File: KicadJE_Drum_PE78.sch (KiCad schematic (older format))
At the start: 112 parts, among them U101 74HC04

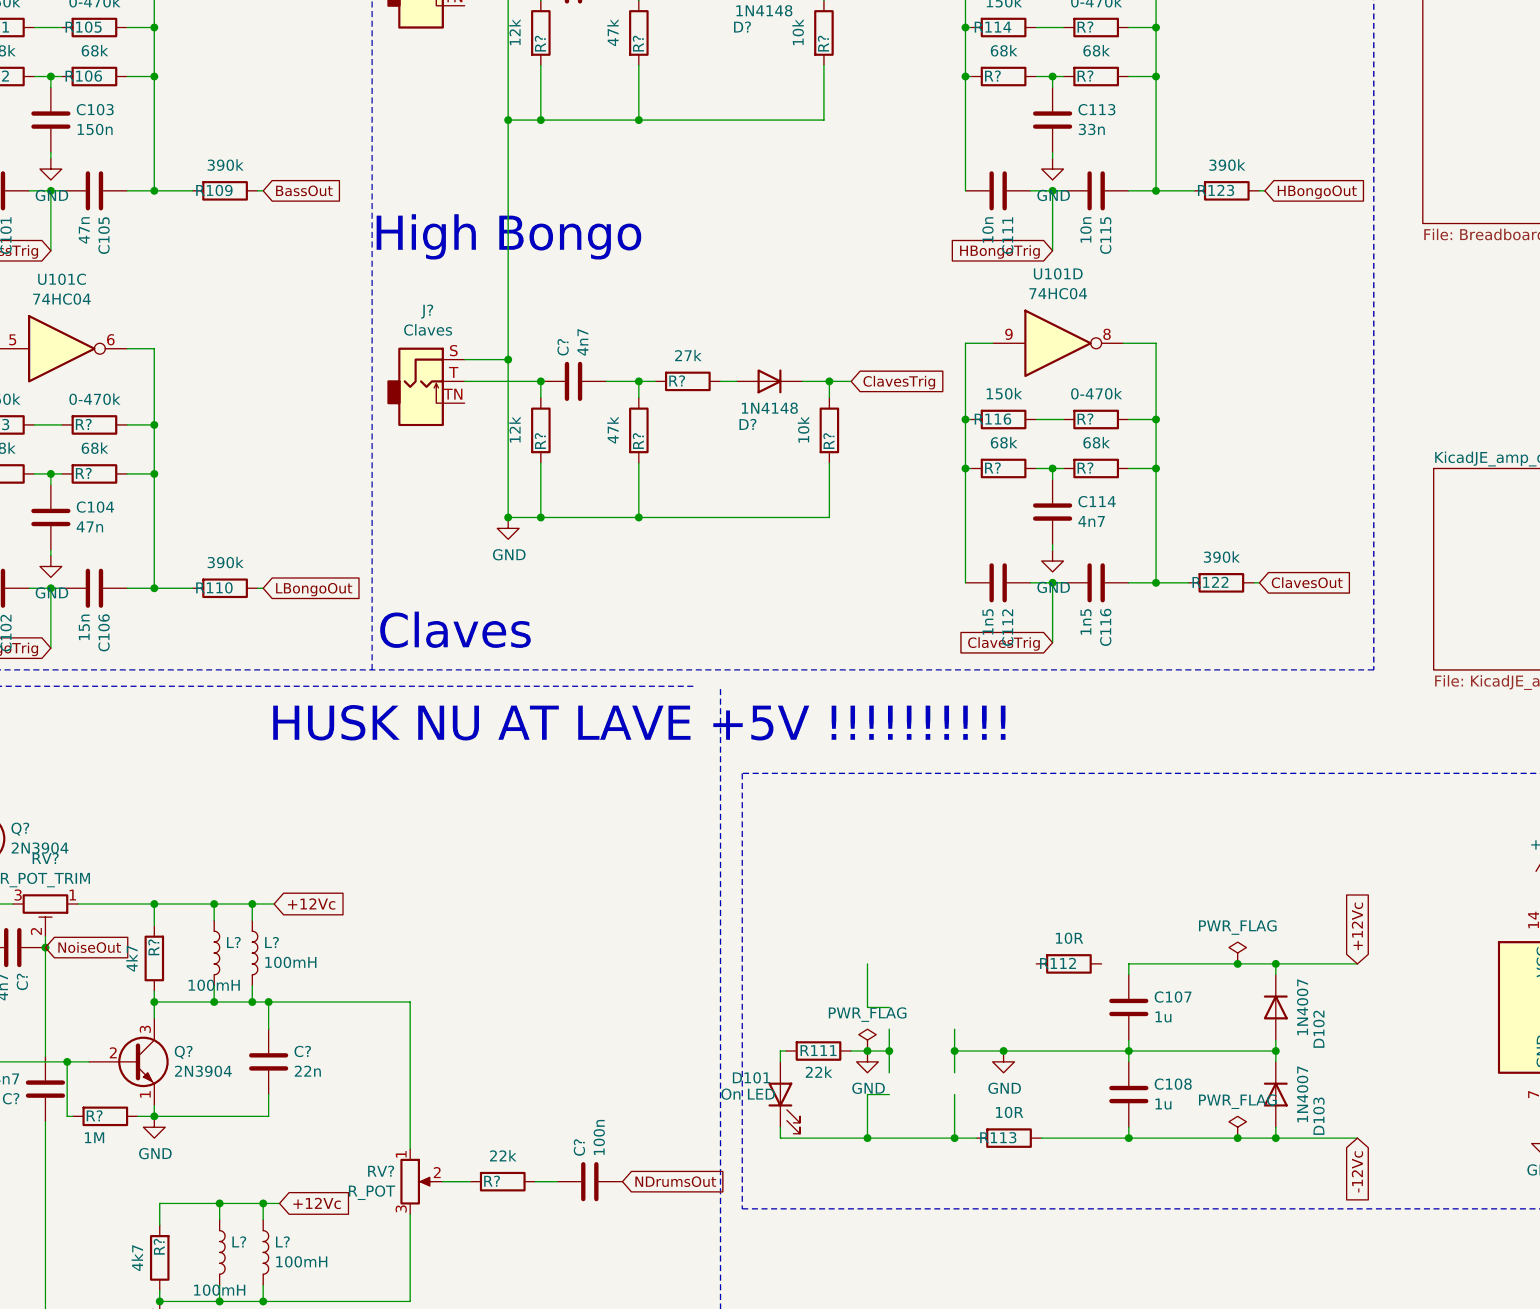
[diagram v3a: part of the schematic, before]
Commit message: Amp out
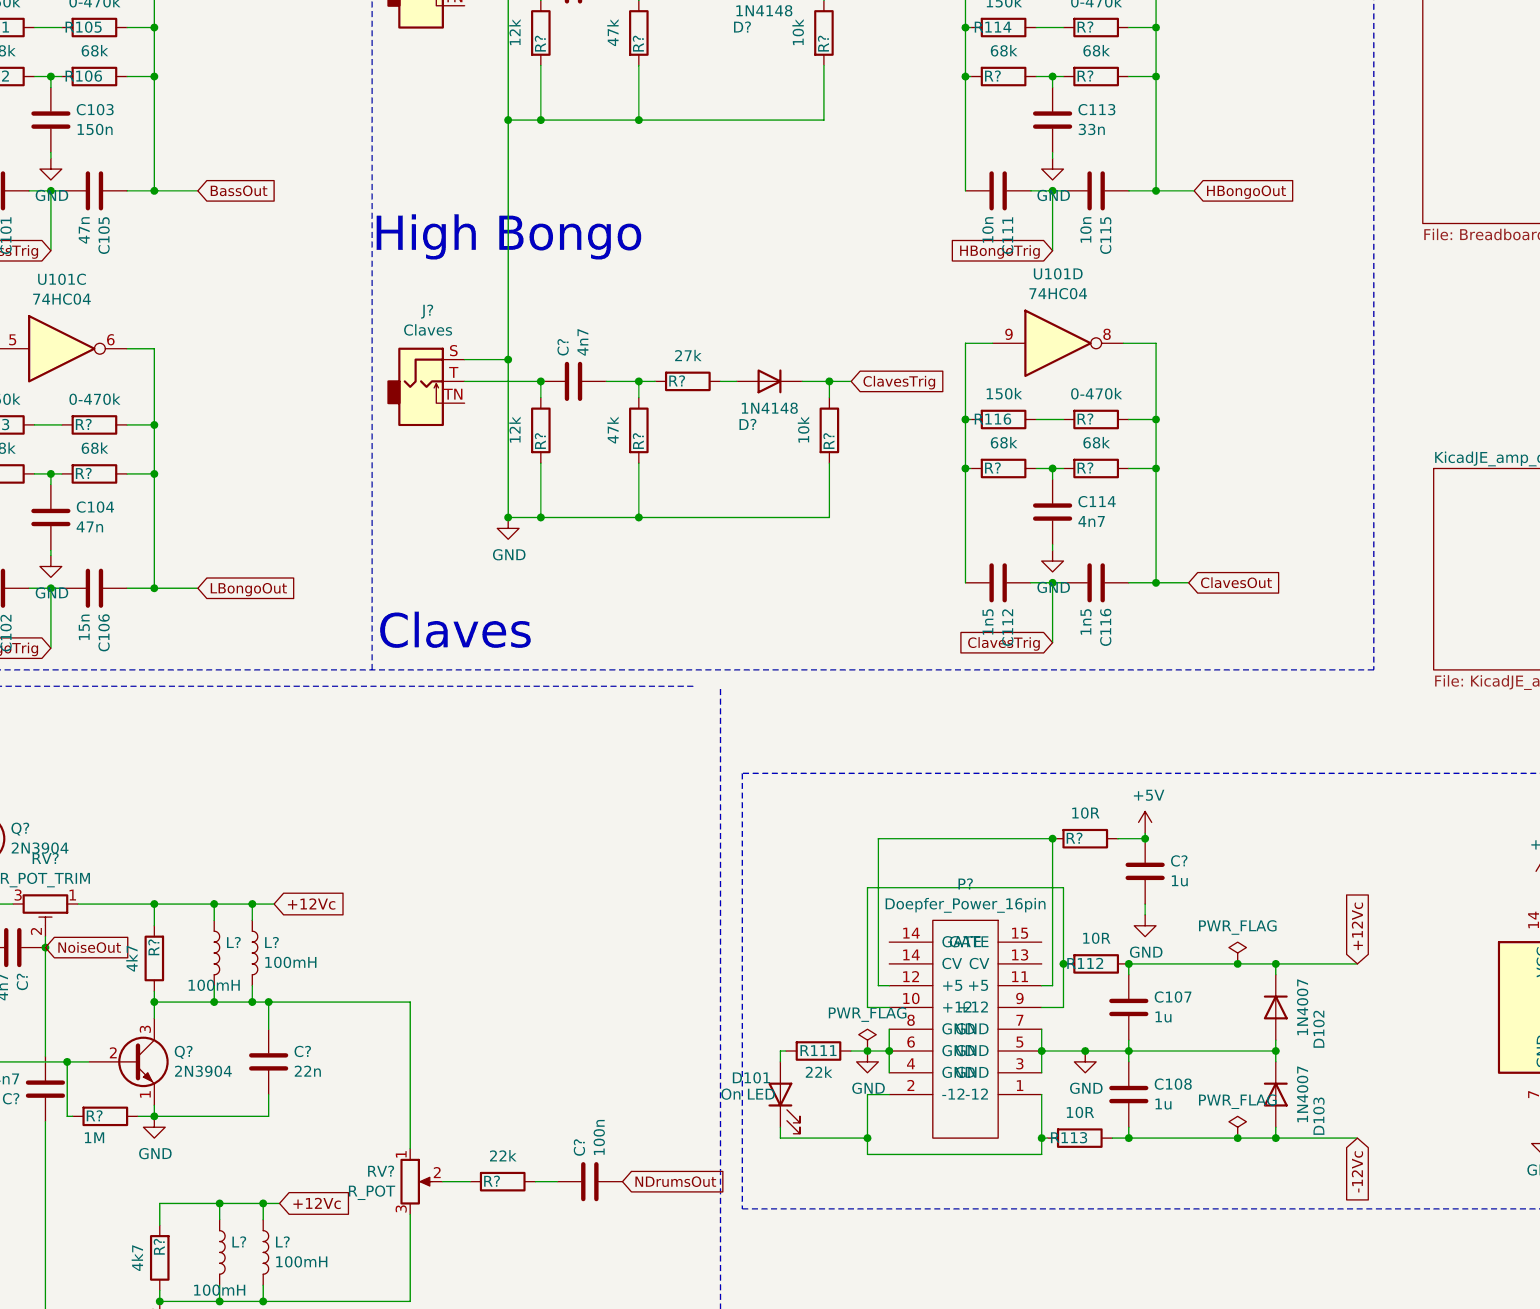
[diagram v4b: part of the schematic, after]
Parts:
- removed R109, R110, R122, R123: 390k, AJ:R_0805_AJ, symbol Device:R
- added C?: 1u, Capacitor_SMD:C_1206_3216Metric_Pad1.42x1.75mm_HandSolder, symbol Device:C
- added P?: Doepfer_Power_16pin, Connector_PinHeader_2.54mm:PinHeader_2x08_P2.54mm_Vertical, symbol Doepfer_Power_14pin:Doepfer_Power_16pin
- added R?: 10R, AJ:R_0805_AJ, symbol Device:R
- RV?: footprint (none) -> AJ:Potentiometer_China_RK09_Single_Vertical_AJ
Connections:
- net +12Vc: now also R112.1
- net +5V: now also C?.1, R?.1
- net BassOut: now also C105.1, R105.1, R106.1, U101.2
- net ClavesOut: now also C116.1, R?.1, R?.1, U101.8
- net GND: now also C?.2, P?.3 (GND), P?.4 (GND), P?.5 (GND), P?.6 (GND), P?.7 (GND), P?.8 (GND)
- net HBongoOut: now also C115.1, R?.1, R?.1, U101.4
- net LBongoOut: now also C106.1, R?.1, R?.1, U101.6
- net at D101.1 (K), R113.2: now also P?.1 (-12), P?.2 (-12)
- net at R112.2: now also P?.10 (+12), P?.9 (+12)
- new net: P?.11 (+5), P?.12 (+5), R?.2
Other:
- moved on the sheet: R112, R113
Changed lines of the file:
@@
 L Device:R R113
 U 1 1 605ABB0A
-P 8225 6175
+P 8550 6175
 AR Path="/605ABB0A" Ref="R113"  Part="1"
 AR Path="/5C8C5FC0/605ABB0A" Ref="R?"  Part="1"
 AR Path="/5D60ED9A/605ABB0A" Ref="R?"  Part="1"
 AR Path="/60565919/605ABB0A" Ref="R?"  Part="1"
-F 0 "R113" V 8225 6125 50  0000 C CNN
-F 1 "10R" V 8109 6175 50  0000 C CNN
-F 2 "AJ:R_0805_AJ" V 8155 6175 50  0001 C CNN
-F 3 "~" H 8225 6175 50  0001 C CNN
-	1    8225 6175
+F 0 "R113" V 8550 6125 50  0000 C CNN
+F 1 "10R" V 8434 6175 50  0000 C CNN
+F 2 "AJ:R_0805_AJ" V 8480 6175 50  0001 C CNN
+F 3 "~" H 8550 6175 50  0001 C CNN
+	1    8550 6175
 	0    1    1    0
 $EndComp
@@
 L Device:R R112
 U 1 1 605ABB10
-P 8500 5375
+P 8625 5375
 AR Path="/605ABB10" Ref="R112"  Part="1"
 AR Path="/5C8C5FC0/605ABB10" Ref="R?"  Part="1"
 AR Path="/5D60ED9A/605ABB10" Ref="R?"  Part="1"
 AR Path="/60565919/605ABB10" Ref="R?"  Part="1"
-F 0 "R112" V 8500 5325 50  0000 C CNN
-F 1 "10R" V 8384 5375 50  0000 C CNN
-F 2 "AJ:R_0805_AJ" V 8430 5375 50  0001 C CNN
-F 3 "~" H 8500 5375 50  0001 C CNN
-	1    8500 5375
+F 0 "R112" V 8625 5325 50  0000 C CNN
+F 1 "10R" V 8509 5375 50  0000 C CNN
+F 2 "AJ:R_0805_AJ" V 8555 5375 50  0001 C CNN
+F 3 "~" H 8625 5375 50  0001 C CNN
+	1    8625 5375
 	0    1    1    0
 $EndComp
@@
 Wire Wire Line
 	7575 5775 7675 5775
-Wire Wire Line
-	7975 5775 8200 5775
 Text GLabel 9825 6175 3    50   Input ~ 0
 -12Vc
@@
 Wire Wire Line
 	8775 5425 8775 5375
-Wire Wire Line
-	8375 6175 8775 6175
-Connection ~ 8775 6175
 Wire Wire Line
 	8775 6125 8775 6175
@@
 $EndComp
 Wire Wire Line
-	7975 6175 8075 6175
-Connection ~ 7975 6175
-Wire Wire Line
-	7975 5975 7975 6175
-Wire Wire Line
-	7975 5775 7975 5675
-Connection ~ 7975 5775
-Wire Wire Line
-	7975 5875 7975 5775
+	8375 5775 8375 5675
+Connection ~ 8375 5775
+Wire Wire Line
+	8375 5875 8375 5775
 Wire Wire Line
 	7675 5775 7675 5675
@@
 	7175 6175 7575 6175
 Wire Wire Line
-	7575 6175 7975 6175
-Connection ~ 7575 6175
-Wire Wire Line
 	7575 5975 7575 6175
 Wire Wire Line
 	7675 5975 7575 5975
-Wire Wire Line
-	7575 5575 7575 5375
 Wire Wire Line
 	7675 5575 7575 5575
@@
 L power:GND #PWR0104
 U 1 1 6076279B
-P 8200 5775
-F 0 "#PWR0104" H 8200 5525 50  0001 C CNN
-F 1 "GND" H 8205 5602 50  0000 C CNN
-F 2 "" H 8200 5775 50  0001 C CNN
-F 3 "" H 8200 5775 50  0001 C CNN
-	1    8200 5775
+P 8575 5775
+F 0 "#PWR0104" H 8575 5525 50  0001 C CNN
+F 1 "GND" H 8580 5602 50  0000 C CNN
+F 2 "" H 8575 5775 50  0001 C CNN
+F 3 "" H 8575 5775 50  0001 C CNN
+	1    8575 5775
 	1    0    0    -1
 $EndComp
@@
 	1    0    0    -1
 $EndComp
-Connection ~ 8200 5775
-Wire Wire Line
-	8200 5775 8775 5775
 $Comp
 L 74xx:74HC04 U101
@@
 Wire Wire Line
 	8425 3625 8325 3625
-Text GLabel 4800 1825 2    47   Input ~ 0
+Text GLabel 4500 1825 2    47   Input ~ 0
 BassOut
-Wire Wire Line
-	4300 1825 4475 1825
 Connection ~ 4300 1825
-$Comp
-L Device:R R109
-U 1 1 607BE08D
-P 4625 1825
-AR Path="/607BE08D" Ref="R109"  Part="1"
-AR Path="/5C8C5FC0/607BE08D" Ref="R?"  Part="1"
-AR Path="/5D60ED9A/607BE08D" Ref="R?"  Part="1"
-AR Path="/60565919/607BE08D" Ref="R?"  Part="1"
-F 0 "R109" V 4625 1775 50  0000 C CNN
-F 1 "390k" V 4509 1825 50  0000 C CNN
-F 2 "AJ:R_0805_AJ" V 4555 1825 50  0001 C CNN
-F 3 "~" H 4625 1825 50  0001 C CNN
-	1    4625 1825
-	0    1    1    0
-$EndComp
-Wire Wire Line
-	4775 1825 4800 1825
 $Comp
 L Device:R R103
@@
 Wire Wire Line
 	3825 3650 3725 3650
-Text GLabel 4800 3650 2    47   Input ~ 0
+Text GLabel 4500 3650 2    47   Input ~ 0
 LBongoOut
-Wire Wire Line
-	4300 3650 4475 3650
 Connection ~ 4300 3650
-$Comp
-L Device:R R110
-U 1 1 607C1D57
-P 4625 3650
-AR Path="/607C1D57" Ref="R110"  Part="1"
-AR Path="/5C8C5FC0/607C1D57" Ref="R?"  Part="1"
-AR Path="/5D60ED9A/607C1D57" Ref="R?"  Part="1"
-AR Path="/60565919/607C1D57" Ref="R?"  Part="1"
-F 0 "R110" V 4625 3600 50  0000 C CNN
-F 1 "390k" V 4509 3650 50  0000 C CNN
-F 2 "AJ:R_0805_AJ" V 4555 3650 50  0001 C CNN
-F 3 "~" H 4625 3650 50  0001 C CNN
-	1    4625 3650
-	0    1    1    0
-$EndComp
-Wire Wire Line
-	4775 3650 4800 3650
 Wire Wire Line
 	3425 2550 3575 2550
 Wire Wire Line
 	4175 2550 4300 2550
-Text GLabel 9400 1825 2    47   Input ~ 0
+Text GLabel 9075 1825 2    47   Input ~ 0
 HBongoOut
 Wire Wire Line
 	8900 1825 9075 1825
-$Comp
-L Device:R R123
-U 1 1 607D73A4
-P 9225 1825
-AR Path="/607D73A4" Ref="R123"  Part="1"
-AR Path="/5C8C5FC0/607D73A4" Ref="R?"  Part="1"
-AR Path="/5D60ED9A/607D73A4" Ref="R?"  Part="1"
-AR Path="/60565919/607D73A4" Ref="R?"  Part="1"
-F 0 "R123" V 9225 1775 50  0000 C CNN
-F 1 "390k" V 9109 1825 50  0000 C CNN
-F 2 "AJ:R_0805_AJ" V 9155 1825 50  0001 C CNN
-F 3 "~" H 9225 1825 50  0001 C CNN
-	1    9225 1825
-	0    1    1    0
-$EndComp
-Wire Wire Line
-	9375 1825 9400 1825
 Connection ~ 8900 1825
 Wire Wire Line
@@
 Wire Wire Line
 	8750 2525 8900 2525
-Text GLabel 9375 3625 2    47   Input ~ 0
+Text GLabel 9050 3625 2    47   Input ~ 0
 ClavesOut
-$Comp
-L Device:R R122
-U 1 1 607F00E5
-P 9200 3625
-AR Path="/607F00E5" Ref="R122"  Part="1"
-AR Path="/5C8C5FC0/607F00E5" Ref="R?"  Part="1"
-AR Path="/5D60ED9A/607F00E5" Ref="R?"  Part="1"
-AR Path="/60565919/607F00E5" Ref="R?"  Part="1"
-F 0 "R122" V 9200 3575 50  0000 C CNN
-F 1 "390k" V 9084 3625 50  0000 C CNN
-F 2 "AJ:R_0805_AJ" V 9130 3625 50  0001 C CNN
-F 3 "~" H 9200 3625 50  0001 C CNN
-	1    9200 3625
-	0    1    1    0
-$EndComp
-Wire Wire Line
-	9350 3625 9375 3625
 Wire Wire Line
 	9050 3625 8900 3625
@@
 $EndComp
 Wire Wire Line
-	8775 5775 9450 5775
-Wire Wire Line
 	8775 5375 9275 5375
 Wire Wire Line
@@
 L power:+5V #PWR?
 U 1 1 60DE30BF
-P 10675 5000
-F 0 "#PWR?" H 10675 4850 50  0001 C CNN
-F 1 "+5V" H 10690 5173 50  0000 C CNN
-F 2 "" H 10675 5000 50  0001 C CNN
-F 3 "" H 10675 5000 50  0001 C CNN
-	1    10675 5000
+P 8850 4775
+F 0 "#PWR?" H 8850 4625 50  0001 C CNN
+F 1 "+5V" H 8865 4948 50  0000 C CNN
+F 2 "" H 8850 4775 50  0001 C CNN
+F 3 "" H 8850 4775 50  0001 C CNN
+	1    8850 4775
 	1    0    0    -1
 $EndComp
@@
 	10675 6150 10675 6075
 Text Notes 5000 8950 0    157  ~ 0
-HUSK NU AT LAVE +5V !!!!!!!!!!
-Text Notes 4825 4375 0    157  ~ 0
 HUSK NU AT LAVE +5V !!!!!!!!!!
 $Comp
@@
 F 0 "RV?" H 5406 6421 50  0000 R CNN
 F 1 "R_POT" H 5406 6330 50  0000 R CNN
-F 2 "" H 5475 6375 50  0001 C CNN
+F 2 "AJ:Potentiometer_China_RK09_Single_Vertical_AJ" H 5475 6375 50  0001 C CNN
 F 3 "~" H 5475 6375 50  0001 C CNN
 	1    5475 6375
@@
 Wire Wire Line
 	4800 6475 4875 6475
+$Comp
+L Doepfer_Power_14pin:Doepfer_Power_16pin P?
+U 1 1 61739A83
+P 8025 5675
+F 0 "P?" H 8025 5010 50  0000 C CNN
+F 1 "Doepfer_Power_16pin" H 8025 5101 50  0000 C CNN
+F 2 "Connector_PinHeader_2.54mm:PinHeader_2x08_P2.54mm_Vertical" H 8025 5675 50  0001 C CNN
+F 3 "DOCUMENTATION" H 8025 5675 50  0001 C CNN
+	1    8025 5675
+	-1   0    0    1
+$EndComp
+Connection ~ 8775 5375
+Wire Wire Line
+	8575 5775 8775 5775
+Wire Wire Line
+	8775 5775 9450 5775
+Wire Wire Line
+	8375 5775 8575 5775
+Connection ~ 8575 5775
+Wire Wire Line
+	8775 6175 8700 6175
+Connection ~ 8775 6175
+Wire Wire Line
+	8400 6175 8375 6175
+Wire Wire Line
+	8375 6175 8375 5975
+Wire Wire Line
+	7575 6175 7575 6250
+Wire Wire Line
+	7575 6250 8375 6250
+Wire Wire Line
+	8375 6250 8375 6175
+Connection ~ 7575 6175
+Connection ~ 8375 6175
+Wire Wire Line
+	8375 5575 8475 5575
+Wire Wire Line
+	8475 5575 8475 5375
+Wire Wire Line
+	7575 5025 8475 5025
+Wire Wire Line
+	8475 5025 8475 5375
+Wire Wire Line
+	7575 5025 7575 5575
+Connection ~ 8475 5375
+$Comp
+L Device:R R?
+U 1 1 619774B5
+P 8575 4800
+AR Path="/619774B5" Ref="R?"  Part="1"
+AR Path="/5C8C5FC0/619774B5" Ref="R?"  Part="1"
+AR Path="/5D60ED9A/619774B5" Ref="R?"  Part="1"
+AR Path="/60565919/619774B5" Ref="R?"  Part="1"
+F 0 "R?" V 8575 4750 50  0000 C CNN
+F 1 "10R" V 8459 4800 50  0000 C CNN
+F 2 "AJ:R_0805_AJ" V 8505 4800 50  0001 C CNN
+F 3 "~" H 8575 4800 50  0001 C CNN
+	1    8575 4800
+	0    1    1    0
+$EndComp
+Wire Wire Line
+	7675 5475 7625 5475
+Wire Wire Line
+	7625 5475 7625 4800
+Wire Wire Line
+	8375 5475 8425 5475
+Wire Wire Line
+	8425 4800 8425 5475
+Connection ~ 8425 4800
+Wire Wire Line
+	7625 4800 8425 4800
+Wire Wire Line
+	8725 4800 8850 4800
+Wire Wire Line
+	8850 4800 8850 4775
+$Comp
+L Device:C C?
+U 1 1 61A3ECD2
+P 8850 4950
+F 0 "C?" H 8965 4996 50  0000 L CNN
+F 1 "1u" H 8965 4905 50  0000 L CNN
+F 2 "Capacitor_SMD:C_1206_3216Metric_Pad1.42x1.75mm_HandSolder" H 8888 4800 50  0001 C CNN
+F 3 "~" H 8850 4950 50  0001 C CNN
+	1    8850 4950
+	1    0    0    -1
+$EndComp
+Connection ~ 8850 4800
+$Comp
+L power:GND #PWR?
+U 1 1 61A3F1FE
+P 8850 5150
+F 0 "#PWR?" H 8850 4900 50  0001 C CNN
+F 1 "GND" H 8855 4977 50  0000 C CNN
+F 2 "" H 8850 5150 50  0001 C CNN
+F 3 "" H 8850 5150 50  0001 C CNN
+	1    8850 5150
+	1    0    0    -1
+$EndComp
+Wire Wire Line
+	8850 5150 8850 5100
+$Comp
+L power:+5V #PWR?
+U 1 1 61A81B6C
+P 10675 5000
+F 0 "#PWR?" H 10675 4850 50  0001 C CNN
+F 1 "+5V" H 10690 5173 50  0000 C CNN
+F 2 "" H 10675 5000 50  0001 C CNN
+F 3 "" H 10675 5000 50  0001 C CNN
+	1    10675 5000
+	1    0    0    -1
+$EndComp
+Wire Wire Line
+	4300 1825 4500 1825
+Wire Wire Line
+	4300 3650 4500 3650
 $EndSCHEMATC

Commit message: Update misc diags
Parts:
- added C?: 100n, Capacitor_SMD:C_1206_3216Metric_Pad1.42x1.75mm_HandSolder, symbol Device:C
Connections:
- net +5V: now also C?.1
- net GND: now also C?.2
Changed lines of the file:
@@
 $EndComp
 Wire Wire Line
-	8850 5150 8850 5100
+	8850 5150 8850 5125
 $Comp
 L power:+5V #PWR?
@@
 Wire Wire Line
 	4300 3650 4500 3650
+$Comp
+L Device:C C?
+U 1 1 608295AC
+P 9200 4950
+F 0 "C?" H 9315 4996 50  0000 L CNN
+F 1 "100n" H 9315 4905 50  0000 L CNN
+F 2 "Capacitor_SMD:C_1206_3216Metric_Pad1.42x1.75mm_HandSolder" H 9238 4800 50  0001 C CNN
+F 3 "~" H 9200 4950 50  0001 C CNN
+	1    9200 4950
+	1    0    0    -1
+$EndComp
+Wire Wire Line
+	8850 4800 9200 4800
+Wire Wire Line
+	9200 5100 9200 5125
+Wire Wire Line
+	9200 5125 8850 5125
+Connection ~ 8850 5125
+Wire Wire Line
+	8850 5125 8850 5100
 $EndSCHEMATC

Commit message: Annotate
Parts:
- gave numbers to parts that had none: 84
- renumbered C101 to C109, C102 to C110, C103 to C113, C104 to C114, C105 to C115, C106 to C116, C111 to C121, C112 to C122, C113 to C123, C114 to C124, C115 to C125, C116 to C126, C107 to C127, C108 to C128, D101 to D109, D102 to D110, D103 to D111, R101 to R119, R102 to R120, R103 to R121, R105 to R124, R106 to R125, R111 to R138, R114 to R141, R116 to R143, R113 to R145, R112 to R151
